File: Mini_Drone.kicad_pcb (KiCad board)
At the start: 4 copper layers, 55 x 50.7 mm, 82 parts, among them J1 Conn_01x02, J3 Conn_01x02, J4 Conn_01x06, J7 Conn_01x11, J8 Conn_01x11, Q1 AO3400A, Q2 AO3400A, Q3 AO3400A, Q4 AO3400A, U1 ESP32-S3-WROOM-1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

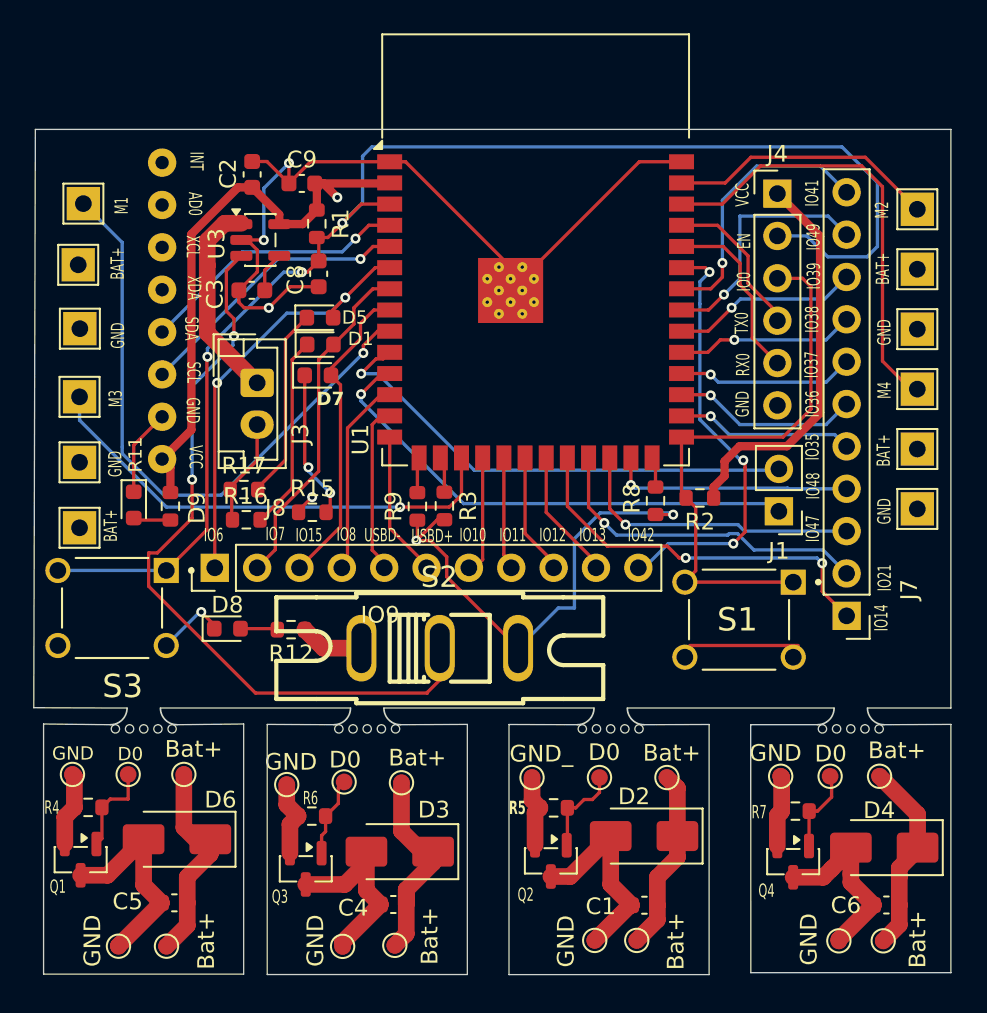
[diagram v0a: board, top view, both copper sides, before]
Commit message: smd pads has been changed to through hole pad and silkscreen has been arranged
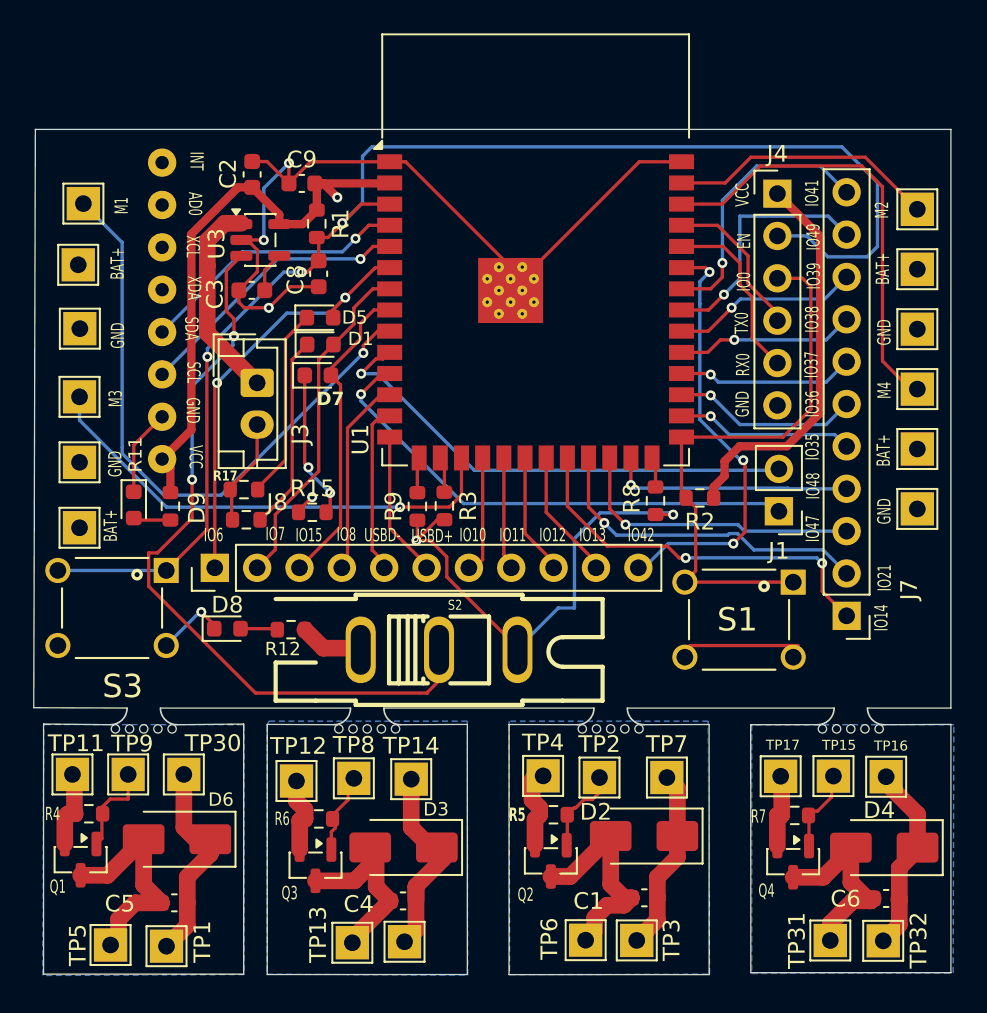
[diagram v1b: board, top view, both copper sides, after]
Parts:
- TP1, TP10, TP11, TP12, TP13, TP14, TP15, TP16, TP17, TP2, TP3, TP30, TP31, TP32, TP4, TP5, TP6, TP7, TP8, TP9: footprint TestPoint:TestPoint_Pad_D1.0mm -> TestPoint:TestPoint_THTPad_2.0x2.0mm_Drill1.0mm
- moved TP4 0.67 mm to (221.4, 110.1)
- moved C4 0.62 mm to (213.1, 117.6)
- moved Q3 0.62 mm to (207.8, 115.4)
- moved TP12 0.62 mm to (206.7, 110.4)
- moved TP10 0.62 mm to (213.1, 120.0)
- moved TP13 0.62 mm to (210.0, 120.1)
- moved TP14 0.62 mm to (213.5, 110.3)
- moved TP8 0.62 mm to (210.1, 110.2)
- moved TP6 0.55 mm to (224.0, 119.9)
- moved TP31 0.52 mm to (238.7, 119.9)
- moved TP5 0.48 mm to (195.5, 120.2)
- moved R6 0.45 mm to (208.0, 112.7)
- moved C1 0.45 mm to (227.5, 117.4)
- moved R5 0.41 mm to (222.1, 112.4)
- moved TP16 0.40 mm to (242.0, 110.1)
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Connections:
- net Net-(Q1-S) renamed /gnd1
- net Net-(Q2-S) renamed /gnd3
- net Net-(Q3-S) renamed /gnd2
- net Net-(Q4-S) renamed /gnd4
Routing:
- net Net-(D6-A): track 12.6 -> 13.6 mm
- net Net-(D2-A): track 12.3 -> 13.3 mm
- net Net-(D4-A): track 11.0 -> 12.0 mm
- net /gnd3: track 4.37 -> 4.98 mm
- added copper zone on B.Cu, net /gnd1
- added copper zone on B.Cu, net /gnd2
- added copper zone on B.Cu, net /gnd3
- added copper zone on B.Cu, net /gnd4
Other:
- board text removed: "IO9"
